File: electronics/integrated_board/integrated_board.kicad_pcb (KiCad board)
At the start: 2 copper layers, 98.5 x 111 mm, 64 parts, among them CON1 BARREL_JACK, J1 rot_encoderZ(35,34), J10 pcf8575 IO expander, J11 Switch 1, J13 motor1(15,2,0,4), J15 motor2 (16,17,5,18), J17 motor3 (19,21,22,23), J2 rot_encoderY(25,26), J3 rot_encoderX(14,27), J4 Switch 2, J5 Endstop A, J6 Endstop B, J7 Endstop C, J8 Conn_01x16, J9 Conn_01x16, P1 Conn_01x02, P10 Conn_01x02, P15 Conn_01x02, P2 LCD, U1 ULN2003, U2 ULN2003, U3 LM2596T-5, U4 ESP32-DEVKITC-32D

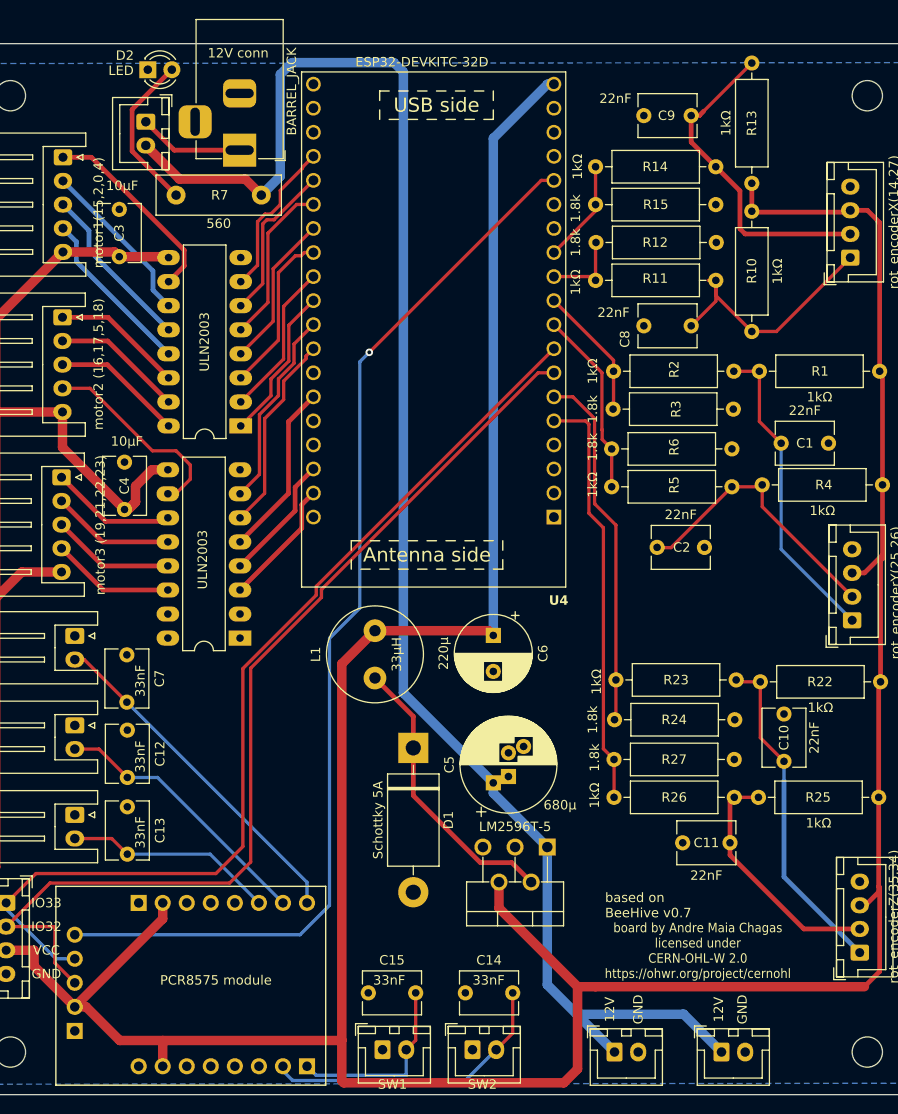
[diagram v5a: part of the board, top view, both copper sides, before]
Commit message: Update PCB
reintroduced push-switches as controlled by individual pins for better use of interrupts
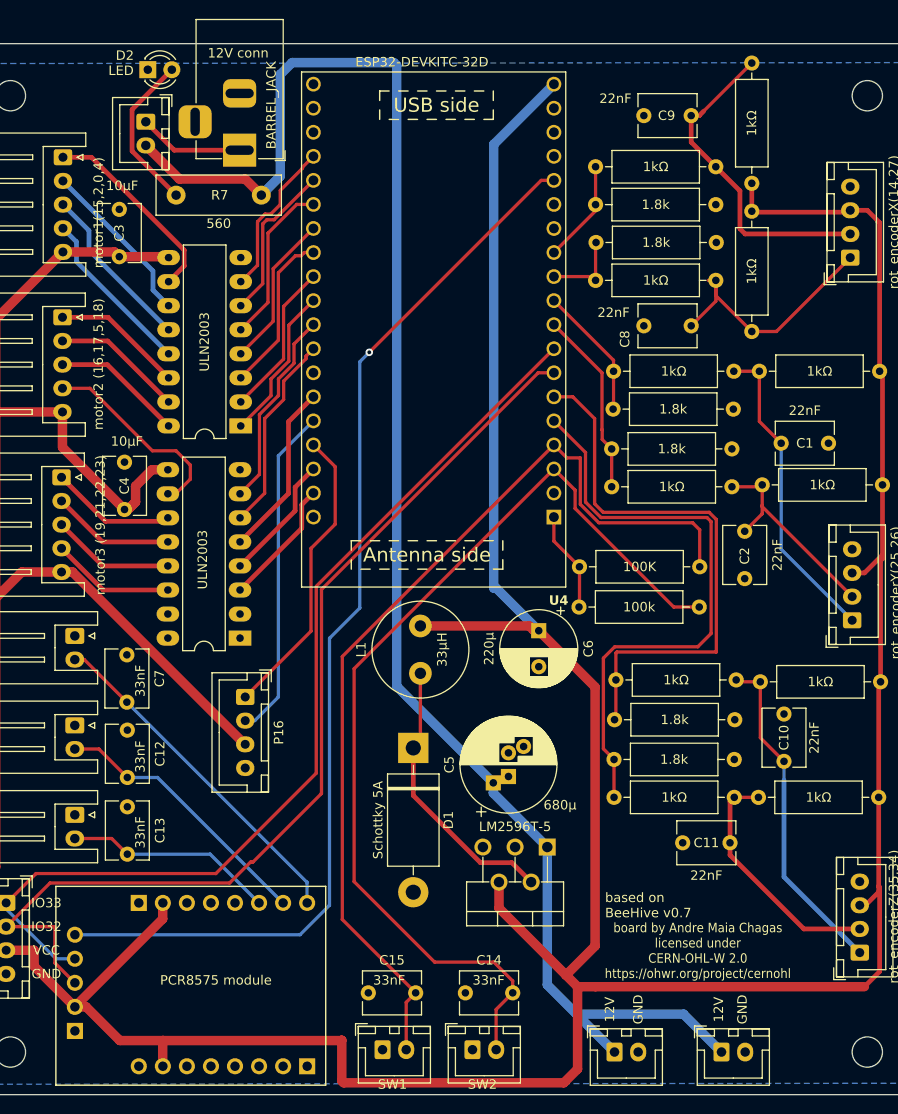
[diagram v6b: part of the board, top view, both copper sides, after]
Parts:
- added P16: UART, Connector_JST:JST_XH_B4B-XH-A_1x04_P2.50mm_Vertical, F.Cu at (123.5, 109.0)
- added R8: 100K, Resistor_THT:R_Axial_DIN0309_L9.0mm_D3.2mm_P12.70mm_Horizontal, F.Cu at (171.5, 95.2)
- added R9: 100k, Resistor_THT:R_Axial_DIN0309_L9.0mm_D3.2mm_P12.70mm_Horizontal, F.Cu at (158.8, 99.5)
- moved C2 5.38 mm to (176.2, 96.5), turned to 90 degrees
- moved C6 4.83 mm to (154.5, 102.0)
- moved L1 4.83 mm to (142.0, 106.5)
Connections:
- net Net-(J10-Pin_3) renamed I2C_SDA
- net Net-(J10-Pin_4) renamed I2C_SCL
- net Net-(J10-Pin_5) renamed I2C_INT
- J8 pad 1: Net-(J11-Pin_2) -> unconnected-(J8-Pin_1-Pad1)
- J8 pad 2: Net-(J4-Pin_2) -> unconnected-(J8-Pin_2-Pad2)
- U4 pad 3: switch2 -> Net-(J4-Pin_2)
- U4 pad 4: switch1 -> Net-(J11-Pin_2)
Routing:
- net Net-(J11-Pin_2): track 20.0 -> 102.6 mm
- net Net-(J4-Pin_2): track 31.5 -> 103.9 mm
- net RX: track 0.00 -> 35.2 mm
- net TX: track 0.00 -> 31.5 mm
- net +5V: track 493.9 -> 517.4 mm
- net encoderZ_1: track 38.0 -> 59.5 mm
- net encoderZ_2: track 44.3 -> 63.5 mm
- net +3V3: track 0.00 -> 10.6 mm
- net Net-(J2-Pin_2): track 29.6 -> 22.5 mm
- net Net-(D1-K): track 30.3 -> 29.5 mm
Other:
- board text removed: "R11"
- board text removed: "R24"
